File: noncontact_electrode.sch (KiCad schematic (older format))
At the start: 10 parts, among them J1 CONN_01, J2 CONN_01, U1 LMP7702MM

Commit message: low impedance verison complete
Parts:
- removed C2: C, Capacitor_SMD:C_0402_1005Metric, symbol Device:C
- removed U1: LMP7702MM, LMP7721MA:SOIC127P600X175-8N, symbol LMP7702MM:LMP7702MM
- added R4: R, Resistor_SMD:R_0402_1005Metric, symbol Device:R
- added U1: LMP7721MA, LMP7721MA:SOIC127P600X175-8N, symbol LMP7721MA:LMP7721MA
- gave numbers to parts that had none: 2
- renumbered J2 to Out1, J1 to Vcc/2
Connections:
- wire segments 26 -> 21
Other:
- moved on the sheet: C1, Out1, R1, R2, R3, Vcc/2
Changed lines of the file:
@@
 $EndDescr
-$Comp
-L LMP7702MM:LMP7702MM U1
-U 1 1 5D4CCAAC
-P 4850 4300
-F 0 "U1" H 4850 4870 50  0000 C CNN
-F 1 "LMP7702MM" H 4850 4779 50  0000 C CNN
-F 2 "LMP7721MA:SOIC127P600X175-8N" H 4850 4300 50  0001 L BNN
-F 3 "" H 4850 4300 50  0001 L BNN
-F 4 "MSOP-8 Texas Instruments" H 4850 4300 50  0001 L BNN "Field4"
-F 5 "LMP7702MM/NOPB" H 4850 4300 50  0001 L BNN "Field5"
-F 6 "Unavailable" H 4850 4300 50  0001 L BNN "Field6"
-F 7 "None" H 4850 4300 50  0001 L BNN "Field7"
-F 8 "Texas Instruments" H 4850 4300 50  0001 L BNN "Field8"
-	1    4850 4300
-	1    0    0    -1
-$EndComp
-Wire Wire Line
-	4150 4300 3900 4300
-Wire Wire Line
-	5550 4100 5650 4100
 $Comp
 L power:VDD #PWR01
 U 1 1 5D4D46FC
-P 4150 3850
-F 0 "#PWR01" H 4150 3700 50  0001 C CNN
-F 1 "VDD" H 4167 4023 50  0000 C CNN
-F 2 "" H 4150 3850 50  0001 C CNN
-F 3 "" H 4150 3850 50  0001 C CNN
-	1    4150 3850
+P 8050 1950
+F 0 "#PWR01" H 8050 1800 50  0001 C CNN
+F 1 "VDD" H 8067 2123 50  0000 C CNN
+F 2 "" H 8050 1950 50  0001 C CNN
+F 3 "" H 8050 1950 50  0001 C CNN
+	1    8050 1950
 	1    0    0    -1
 $EndComp
@@
 L power:GND #PWR02
 U 1 1 5D4D5611
-P 4150 4950
-F 0 "#PWR02" H 4150 4700 50  0001 C CNN
-F 1 "GND" H 4155 4777 50  0000 C CNN
-F 2 "" H 4150 4950 50  0001 C CNN
-F 3 "" H 4150 4950 50  0001 C CNN
-	1    4150 4950
-	1    0    0    -1
-$EndComp
-Wire Wire Line
-	4150 4100 4150 3850
-Wire Wire Line
-	4150 4800 4150 4950
+P 8050 3250
+F 0 "#PWR02" H 8050 3000 50  0001 C CNN
+F 1 "GND" H 8055 3077 50  0000 C CNN
+F 2 "" H 8050 3250 50  0001 C CNN
+F 3 "" H 8050 3250 50  0001 C CNN
+	1    8050 3250
+	1    0    0    -1
+$EndComp
+Wire Wire Line
+	8050 2200 8050 1950
+Wire Wire Line
+	8050 3100 8050 3250
 $Comp
 L Device:R R3
 U 1 1 5D4D5E2E
-P 6350 4200
-F 0 "R3" V 6143 4200 50  0000 C CNN
-F 1 "R" V 6234 4200 50  0000 C CNN
-F 2 "Resistor_SMD:R_0402_1005Metric" V 6280 4200 50  0001 C CNN
-F 3 "~" H 6350 4200 50  0001 C CNN
-	1    6350 4200
-	0    1    1    0
-$EndComp
-Wire Wire Line
-	5650 4100 5650 3550
-Wire Wire Line
-	5650 3550 3950 3550
-Wire Wire Line
-	3950 3550 3950 4400
-Wire Wire Line
-	3950 4400 4150 4400
-Connection ~ 5650 4100
-Wire Wire Line
-	5650 4100 5800 4100
-Wire Wire Line
-	5550 4200 5700 4200
-Wire Wire Line
-	5700 4200 5700 5250
-Wire Wire Line
-	5700 5250 3950 5250
-Wire Wire Line
-	3950 5250 3950 4500
-Wire Wire Line
-	3950 4500 4150 4500
-Connection ~ 5700 4200
-Wire Wire Line
-	5700 4200 6200 4200
+P 9100 3800
+F 0 "R3" V 8893 3800 50  0000 C CNN
+F 1 "R" V 8984 3800 50  0000 C CNN
+F 2 "Resistor_SMD:R_0402_1005Metric" V 9030 3800 50  0001 C CNN
+F 3 "~" H 9100 3800 50  0001 C CNN
+	1    9100 3800
+	0    -1   -1   0
+$EndComp
 $Comp
 L Device:C C1
 U 1 1 5D4DB760
-P 3750 4300
-F 0 "C1" V 3498 4300 50  0000 C CNN
-F 1 "C" V 3589 4300 50  0000 C CNN
-F 2 "Capacitor_SMD:C_0402_1005Metric" H 3788 4150 50  0001 C CNN
-F 3 "~" H 3750 4300 50  0001 C CNN
-	1    3750 4300
+P 8800 4600
+F 0 "C1" V 8548 4600 50  0000 C CNN
+F 1 "C" V 8639 4600 50  0000 C CNN
+F 2 "Capacitor_SMD:C_0402_1005Metric" H 8838 4450 50  0001 C CNN
+F 3 "~" H 8800 4600 50  0001 C CNN
+	1    8800 4600
 	0    1    1    0
 $EndComp
 $Comp
-L Device:C C2
-U 1 1 5D4DC5BC
-P 6000 4100
-F 0 "C2" V 5748 4100 50  0000 C CNN
-F 1 "C" V 5839 4100 50  0000 C CNN
-F 2 "Capacitor_SMD:C_0402_1005Metric" H 6038 3950 50  0001 C CNN
-F 3 "~" H 6000 4100 50  0001 C CNN
-	1    6000 4100
-	0    1    1    0
-$EndComp
-$Comp
-L SparkFun-Connectors:CONN_01 J1
+L SparkFun-Connectors:CONN_01 Vcc/2
 U 1 1 5D4DD422
-P 6150 3450
-F 0 "J1" V 6013 3528 45  0000 L CNN
-F 1 "CONN_01" V 6097 3528 45  0000 L CNN
-F 2 "digikey-footprints:PROBE_PAD_0603" H 6150 3650 20  0001 C CNN
-F 3 "" H 6150 3450 50  0001 C CNN
-F 4 "XXX-00000" V 6192 3528 60  0000 L CNN "Field4"
-	1    6150 3450
-	0    1    1    0
+P 7400 2400
+F 0 "Vcc/2" V 7263 2478 45  0000 L CNN
+F 1 "CONN_01" V 7347 2478 45  0000 L CNN
+F 2 "digikey-footprints:PROBE_PAD_0603" H 7400 2600 20  0001 C CNN
+F 3 "" H 7400 2400 50  0001 C CNN
+F 4 "XXX-00000" V 7442 2478 60  0000 L CNN "Field4"
+	1    7400 2400
+	1    0    0    -1
 $EndComp
 $Comp
 L Device:R R2
 U 1 1 5D4E1F59
-P 6150 3700
-F 0 "R2" H 6080 3654 50  0000 R CNN
-F 1 "R" H 6080 3745 50  0000 R CNN
-F 2 "Resistor_SMD:R_0402_1005Metric" V 6080 3700 50  0001 C CNN
-F 3 "~" H 6150 3700 50  0001 C CNN
-	1    6150 3700
+P 8450 3800
+F 0 "R2" H 8380 3754 50  0000 R CNN
+F 1 "R" H 8380 3845 50  0000 R CNN
+F 2 "Resistor_SMD:R_0402_1005Metric" V 8380 3800 50  0001 C CNN
+F 3 "~" H 8450 3800 50  0001 C CNN
+	1    8450 3800
+	0    -1   -1   0
+$EndComp
+$Comp
+L SparkFun-Connectors:CONN_01 Out1
+U 1 1 5D4E4202
+P 10000 2200
+F 0 "Out1" H 9958 1890 45  0000 C CNN
+F 1 "CONN_01" H 9958 1974 45  0000 C CNN
+F 2 "digikey-footprints:PROBE_PAD_0603" H 10000 2400 20  0001 C CNN
+F 3 "" H 10000 2200 50  0001 C CNN
+F 4 "XXX-00000" H 9958 2069 60  0000 C CNN "Field4"
+	1    10000 2200
 	-1   0    0    1
 $EndComp
-Wire Wire Line
-	6150 3850 6150 3950
-Wire Wire Line
-	6150 3950 6600 3950
-Wire Wire Line
-	6600 3950 6600 5500
-Wire Wire Line
-	6600 5500 3800 5500
-Wire Wire Line
-	3800 5500 3800 4600
-Wire Wire Line
-	3800 4600 4150 4600
-Connection ~ 6150 3950
-Wire Wire Line
-	6150 3950 6150 4100
-$Comp
-L SparkFun-Connectors:CONN_01 J2
-U 1 1 5D4E4202
-P 7000 4200
-F 0 "J2" H 6958 3890 45  0000 C CNN
-F 1 "CONN_01" H 6958 3974 45  0000 C CNN
-F 2 "digikey-footprints:PROBE_PAD_0603" H 7000 4400 20  0001 C CNN
-F 3 "" H 7000 4200 50  0001 C CNN
-F 4 "XXX-00000" H 6958 4069 60  0000 C CNN "Field4"
-	1    7000 4200
-	-1   0    0    1
-$EndComp
-Wire Wire Line
-	6500 4200 6900 4200
 $Comp
 L Device:R R1
 U 1 1 5D4E5844
-P 5800 3950
-F 0 "R1" H 5730 3904 50  0000 R CNN
-F 1 "R" H 5730 3995 50  0000 R CNN
-F 2 "Resistor_SMD:R_0402_1005Metric" V 5730 3950 50  0001 C CNN
-F 3 "~" H 5800 3950 50  0001 C CNN
-	1    5800 3950
+P 9450 2050
+F 0 "R1" H 9380 2004 50  0000 R CNN
+F 1 "R" H 9380 2095 50  0000 R CNN
+F 2 "Resistor_SMD:R_0402_1005Metric" V 9380 2050 50  0001 C CNN
+F 3 "~" H 9450 2050 50  0001 C CNN
+	1    9450 2050
 	-1   0    0    1
 $EndComp
-Connection ~ 5800 4100
-Wire Wire Line
-	5800 4100 5850 4100
-Wire Wire Line
-	5800 3800 5800 3050
-Wire Wire Line
-	5800 3050 5500 3050
-$Comp
-L power:VDD #PWR?
+$Comp
+L power:VDD #PWR03
 U 1 1 5D4D44AB
 P 3000 2700
-F 0 "#PWR?" H 3000 2550 50  0001 C CNN
+F 0 "#PWR03" H 3000 2550 50  0001 C CNN
 F 1 "VDD" H 3017 2873 50  0000 C CNN
 F 2 "" H 3000 2700 50  0001 C CNN
@@
 $EndComp
 $Comp
-L SparkFun-Connectors:CONN_01 J?
+L SparkFun-Connectors:CONN_01 Vcc1
 U 1 1 5D4D4769
 P 3000 2800
-F 0 "J?" V 2863 2878 45  0000 L CNN
+F 0 "Vcc1" V 2863 2878 45  0000 L CNN
 F 1 "CONN_01" V 2947 2878 45  0000 L CNN
 F 2 "digikey-footprints:PROBE_PAD_0603" H 3000 3000 20  0001 C CNN
@@
 $EndComp
 $Comp
-L power:GND #PWR?
+L power:GND #PWR04
 U 1 1 5D4D54F7
 P 3450 2800
-F 0 "#PWR?" H 3450 2550 50  0001 C CNN
+F 0 "#PWR04" H 3450 2550 50  0001 C CNN
 F 1 "GND" H 3455 2627 50  0000 C CNN
 F 2 "" H 3450 2800 50  0001 C CNN
@@
 $EndComp
 $Comp
-L SparkFun-Connectors:CONN_01 J?
+L SparkFun-Connectors:CONN_01 Gnd1
 U 1 1 5D4D5D37
 P 3450 2700
-F 0 "J?" V 3313 2778 45  0000 L CNN
+F 0 "Gnd1" V 3313 2778 45  0000 L CNN
 F 1 "CONN_01" V 3397 2778 45  0000 L CNN
 F 2 "digikey-footprints:PROBE_PAD_0603" H 3450 2900 20  0001 C CNN
@@
 	0    1    1    0
 $EndComp
+$Comp
+L LMP7721MA:LMP7721MA U1
+U 1 1 5D4D93A5
+P 8750 2500
+F 0 "U1" H 8750 3170 50  0000 C CNN
+F 1 "LMP7721MA" H 8750 3079 50  0000 C CNN
+F 2 "LMP7721MA:SOIC127P600X175-8N" H 8750 2500 50  0001 L BNN
+F 3 "" H 8750 2500 50  0001 L BNN
+F 4 "SOIC-8 Texas Instruments" H 8750 2500 50  0001 L BNN "Field4"
+F 5 "LMP7721MA" H 8750 2500 50  0001 L BNN "Field5"
+F 6 "Unavailable" H 8750 2500 50  0001 L BNN "Field6"
+F 7 "None" H 8750 2500 50  0001 L BNN "Field7"
+F 8 "Texas Instruments" H 8750 2500 50  0001 L BNN "Field8"
+	1    8750 2500
+	1    0    0    -1
+$EndComp
+Wire Wire Line
+	9450 2200 9750 2200
+Connection ~ 9450 2200
+Wire Wire Line
+	7500 2400 7600 2400
+$Comp
+L Device:R R4
+U 1 1 5D4E2791
+P 8800 3950
+F 0 "R4" V 8593 3950 50  0000 C CNN
+F 1 "R" V 8684 3950 50  0000 C CNN
+F 2 "Resistor_SMD:R_0402_1005Metric" V 8730 3950 50  0001 C CNN
+F 3 "~" H 8800 3950 50  0001 C CNN
+	1    8800 3950
+	1    0    0    -1
+$EndComp
+Wire Wire Line
+	8600 3800 8800 3800
+Wire Wire Line
+	8950 3800 8800 3800
+Connection ~ 8800 3800
+Wire Wire Line
+	8050 2500 7750 2500
+Wire Wire Line
+	7750 2500 7750 3800
+Wire Wire Line
+	7750 3800 8250 3800
+Wire Wire Line
+	8250 3800 8250 4600
+Wire Wire Line
+	8250 4600 8650 4600
+Connection ~ 8250 3800
+Wire Wire Line
+	8250 3800 8300 3800
+Wire Wire Line
+	9250 3800 9250 4600
+Wire Wire Line
+	9250 4600 8950 4600
+Wire Wire Line
+	9750 2200 9750 3800
+Wire Wire Line
+	9750 3800 9250 3800
+Connection ~ 9750 2200
+Wire Wire Line
+	9750 2200 9900 2200
+Connection ~ 9250 3800
+Wire Wire Line
+	7200 3800 7750 3800
+Connection ~ 7750 3800
+Wire Wire Line
+	7600 2400 7600 4100
+Wire Wire Line
+	7600 4100 8800 4100
+Connection ~ 7600 2400
+Wire Wire Line
+	7600 2400 8050 2400
 $EndSCHEMATC

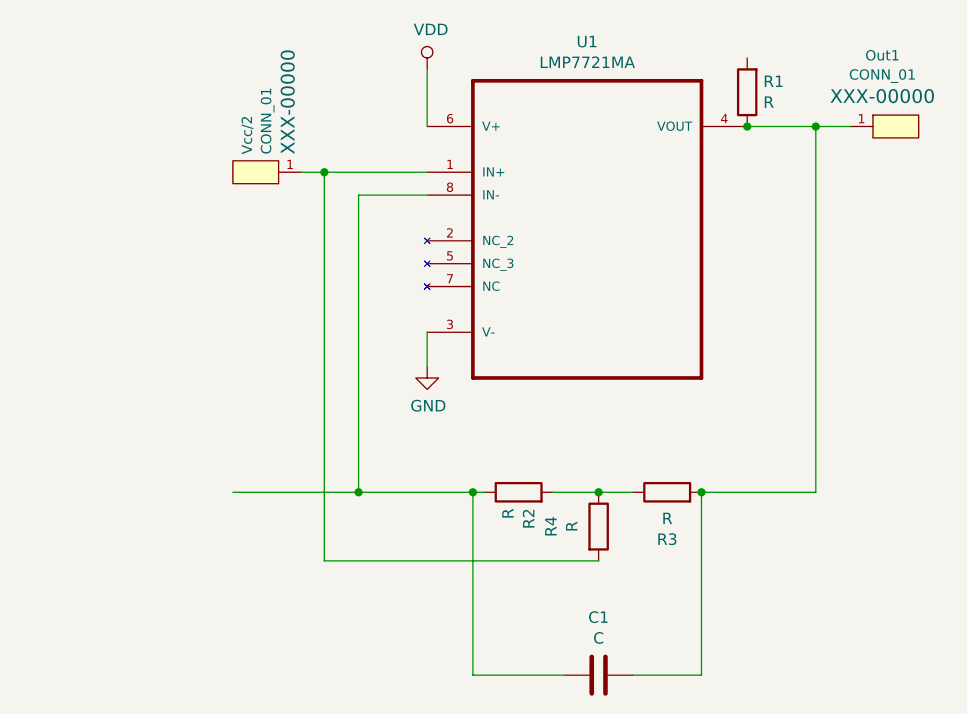
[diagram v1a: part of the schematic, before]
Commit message: high impedance done
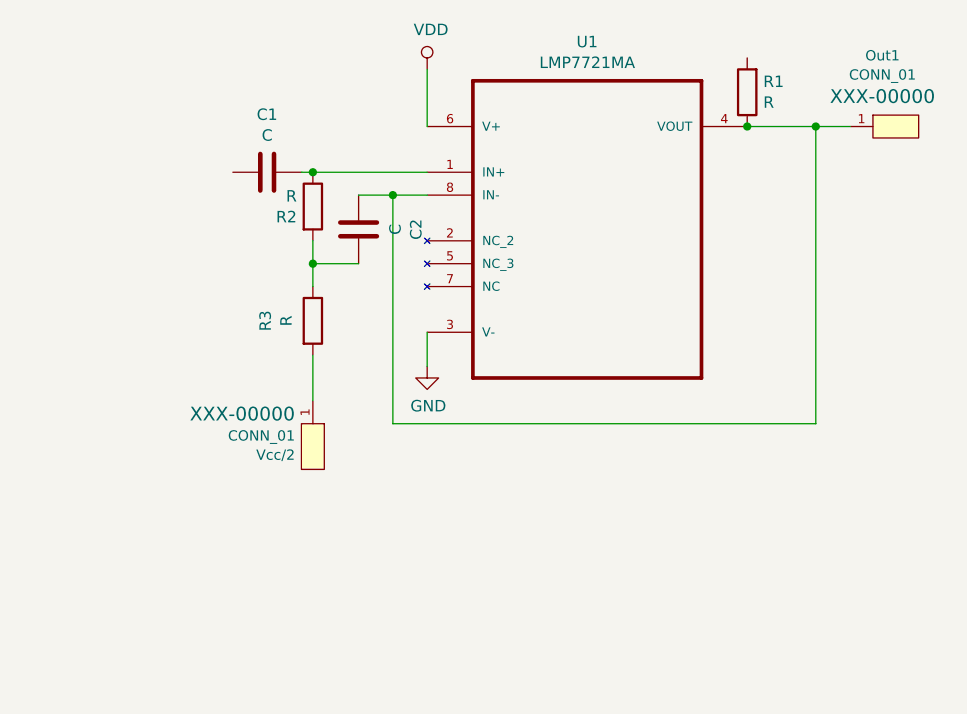
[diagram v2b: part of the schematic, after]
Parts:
- removed R4: R, Resistor_SMD:R_0402_1005Metric, symbol Device:R
- added C2: C, Capacitor_SMD:C_0402_1005Metric, symbol Device:C
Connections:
- wire segments 21 -> 15
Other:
- moved on the sheet: C1, R2, R3, Vcc/2
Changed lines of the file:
@@
 L Device:R R3
 U 1 1 5D4D5E2E
-P 9100 3800
-F 0 "R3" V 8893 3800 50  0000 C CNN
-F 1 "R" V 8984 3800 50  0000 C CNN
-F 2 "Resistor_SMD:R_0402_1005Metric" V 9030 3800 50  0001 C CNN
-F 3 "~" H 9100 3800 50  0001 C CNN
-	1    9100 3800
-	0    -1   -1   0
+P 7550 3050
+F 0 "R3" V 7343 3050 50  0000 C CNN
+F 1 "R" V 7434 3050 50  0000 C CNN
+F 2 "Resistor_SMD:R_0402_1005Metric" V 7480 3050 50  0001 C CNN
+F 3 "~" H 7550 3050 50  0001 C CNN
+	1    7550 3050
+	1    0    0    -1
 $EndComp
 $Comp
 L Device:C C1
 U 1 1 5D4DB760
-P 8800 4600
-F 0 "C1" V 8548 4600 50  0000 C CNN
-F 1 "C" V 8639 4600 50  0000 C CNN
-F 2 "Capacitor_SMD:C_0402_1005Metric" H 8838 4450 50  0001 C CNN
-F 3 "~" H 8800 4600 50  0001 C CNN
-	1    8800 4600
+P 7350 2400
+F 0 "C1" V 7098 2400 50  0000 C CNN
+F 1 "C" V 7189 2400 50  0000 C CNN
+F 2 "Capacitor_SMD:C_0402_1005Metric" H 7388 2250 50  0001 C CNN
+F 3 "~" H 7350 2400 50  0001 C CNN
+	1    7350 2400
 	0    1    1    0
 $EndComp
@@
 L SparkFun-Connectors:CONN_01 Vcc/2
 U 1 1 5D4DD422
-P 7400 2400
-F 0 "Vcc/2" V 7263 2478 45  0000 L CNN
-F 1 "CONN_01" V 7347 2478 45  0000 L CNN
-F 2 "digikey-footprints:PROBE_PAD_0603" H 7400 2600 20  0001 C CNN
-F 3 "" H 7400 2400 50  0001 C CNN
-F 4 "XXX-00000" V 7442 2478 60  0000 L CNN "Field4"
-	1    7400 2400
-	1    0    0    -1
+P 7550 3500
+F 0 "Vcc/2" V 7413 3578 45  0000 L CNN
+F 1 "CONN_01" V 7497 3578 45  0000 L CNN
+F 2 "digikey-footprints:PROBE_PAD_0603" H 7550 3700 20  0001 C CNN
+F 3 "" H 7550 3500 50  0001 C CNN
+F 4 "XXX-00000" V 7592 3578 60  0000 L CNN "Field4"
+	1    7550 3500
+	0    -1   -1   0
 $EndComp
 $Comp
 L Device:R R2
 U 1 1 5D4E1F59
-P 8450 3800
-F 0 "R2" H 8380 3754 50  0000 R CNN
-F 1 "R" H 8380 3845 50  0000 R CNN
-F 2 "Resistor_SMD:R_0402_1005Metric" V 8380 3800 50  0001 C CNN
-F 3 "~" H 8450 3800 50  0001 C CNN
-	1    8450 3800
-	0    -1   -1   0
+P 7550 2550
+F 0 "R2" H 7480 2504 50  0000 R CNN
+F 1 "R" H 7480 2595 50  0000 R CNN
+F 2 "Resistor_SMD:R_0402_1005Metric" V 7480 2550 50  0001 C CNN
+F 3 "~" H 7550 2550 50  0001 C CNN
+	1    7550 2550
+	1    0    0    -1
 $EndComp
 $Comp
@@
 Connection ~ 9450 2200
 Wire Wire Line
-	7500 2400 7600 2400
-$Comp
-L Device:R R4
-U 1 1 5D4E2791
-P 8800 3950
-F 0 "R4" V 8593 3950 50  0000 C CNN
-F 1 "R" V 8684 3950 50  0000 C CNN
-F 2 "Resistor_SMD:R_0402_1005Metric" V 8730 3950 50  0001 C CNN
-F 3 "~" H 8800 3950 50  0001 C CNN
-	1    8800 3950
-	1    0    0    -1
-$EndComp
+	8050 2500 7900 2500
 Wire Wire Line
-	8600 3800 8800 3800
-Wire Wire Line
-	8950 3800 8800 3800
-Connection ~ 8800 3800
-Wire Wire Line
-	8050 2500 7750 2500
-Wire Wire Line
-	7750 2500 7750 3800
-Wire Wire Line
-	7750 3800 8250 3800
-Wire Wire Line
-	8250 3800 8250 4600
-Wire Wire Line
-	8250 4600 8650 4600
-Connection ~ 8250 3800
-Wire Wire Line
-	8250 3800 8300 3800
-Wire Wire Line
-	9250 3800 9250 4600
-Wire Wire Line
-	9250 4600 8950 4600
-Wire Wire Line
-	9750 2200 9750 3800
-Wire Wire Line
-	9750 3800 9250 3800
+	9750 2200 9750 3500
 Connection ~ 9750 2200
 Wire Wire Line
 	9750 2200 9900 2200
-Connection ~ 9250 3800
+$Comp
+L Device:C C2
+U 1 1 5D4D5605
+P 7750 2650
+F 0 "C2" V 7498 2650 50  0000 C CNN
+F 1 "C" V 7589 2650 50  0000 C CNN
+F 2 "Capacitor_SMD:C_0402_1005Metric" H 7788 2500 50  0001 C CNN
+F 3 "~" H 7750 2650 50  0001 C CNN
+	1    7750 2650
+	-1   0    0    1
+$EndComp
 Wire Wire Line
-	7200 3800 7750 3800
-Connection ~ 7750 3800
+	8050 2400 7550 2400
+Connection ~ 7550 2400
 Wire Wire Line
-	7600 2400 7600 4100
+	7550 2400 7500 2400
 Wire Wire Line
-	7600 4100 8800 4100
-Connection ~ 7600 2400
+	7550 2700 7550 2800
 Wire Wire Line
-	7600 2400 8050 2400
+	7750 2800 7550 2800
+Connection ~ 7550 2800
+Wire Wire Line
+	7550 2800 7550 2900
+Wire Wire Line
+	7550 3200 7550 3400
+Wire Wire Line
+	7900 2500 7900 3500
+Wire Wire Line
+	7900 3500 9750 3500
+Connection ~ 7900 2500
+Wire Wire Line
+	7900 2500 7750 2500
 $EndSCHEMATC
